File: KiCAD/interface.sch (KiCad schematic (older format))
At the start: 32 parts, among them P10 C3SB, P11 VSel_Vlv, P14 X_VALVE, P17 PUMP, P18 Pump_Cable, P34 VSel_Vlv2, P38 X_VALVE2, P7 GAGE_PR, P9 C3SB, Q1 BCP5416TA, Q2 BCP5416TA, Q3 BCP5416TA, Q4 BCP5416TA, U1 TXB0104D

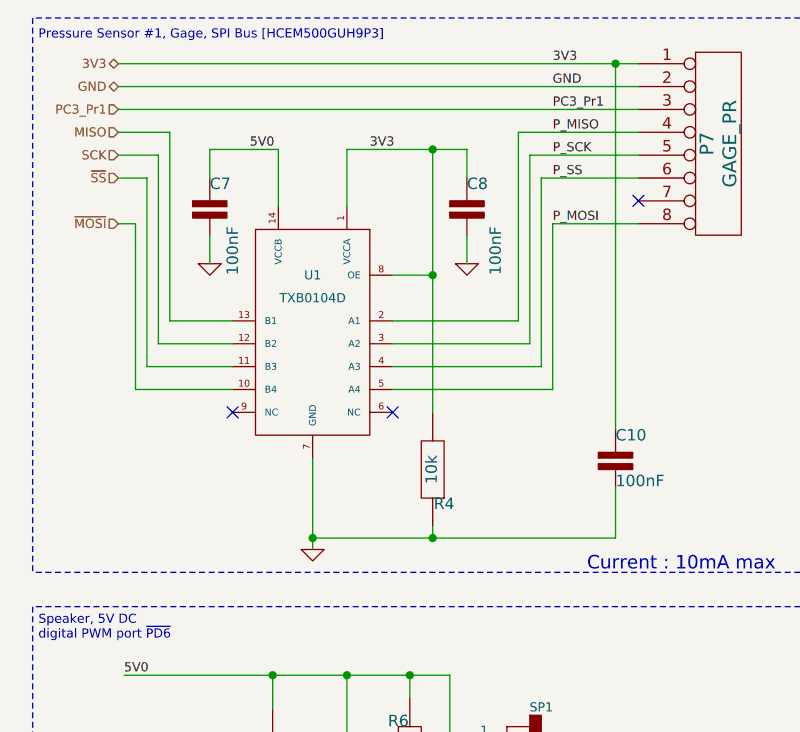
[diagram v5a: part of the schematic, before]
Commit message: layout finalized, needs a check for errors
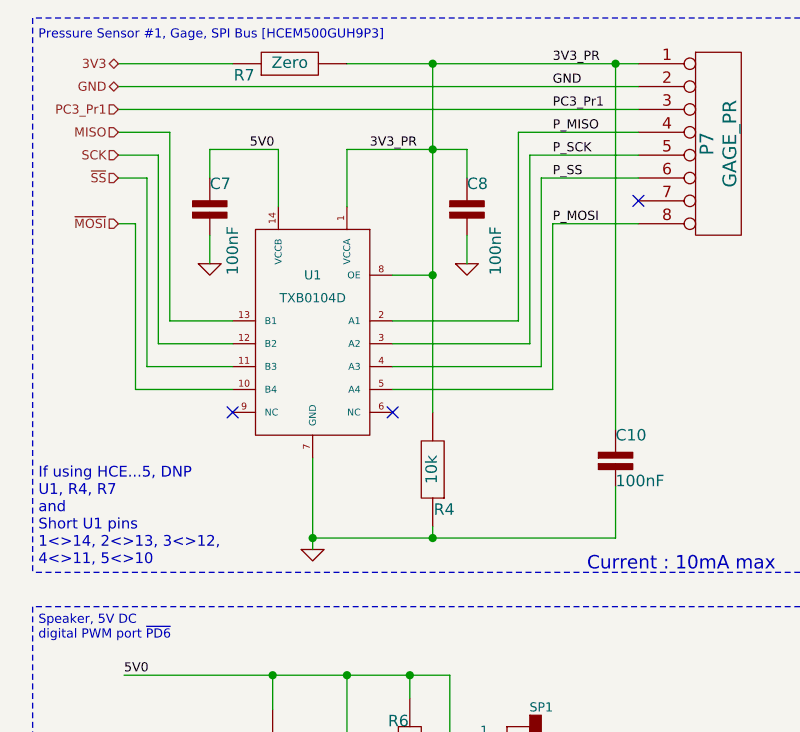
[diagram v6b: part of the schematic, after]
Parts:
- added R7: Zero, uCm:r_0805, symbol R
- U1: footprint uCm:TXB0104D -> uCm:TXB0104D_null
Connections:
- net 3V3: now also R7.1; no longer C10.1, C8.1, P7.1 (P1), R4.2, U1.1 (VCCA), U1.8 (OE)
- new net 3V3_PR: C10.1, C8.1, P7.1 (P1), R4.2, R7.2, U1.1 (VCCA), U1.8 (OE)
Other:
- note added: "If using HCE...5, DNP\nU1, R4, R7\nand\nShort U1 pins\n1<>14, 2<>13, 3<>12, \n4<>11, 5<>10"
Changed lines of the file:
@@
 	3325 875  1050 875
-Wire Wire Line
-	1050 775  3325 775
 Wire Wire Line
 	1050 975  3325 975
@@
 	1450 1525 1450 1650
 Wire Wire Line
-	2425 1150 2425 2300
+	2425 775  2425 2300
 Connection ~ 2425 1700
 Wire Notes Line
@@
 F 0 "U1" H 1900 2500 40  0000 C CNN
 F 1 "TXB0104D" H 1900 2400 40  0000 C CNN
-F 2 "uCm:TXB0104D" H 1900 2500 40  0001 C CNN
+F 2 "uCm:TXB0104D_null" H 1900 2500 40  0001 C CNN
 F 3 "" H 1900 2100 60  0001 C CNN
 F 4 "TXB0104DR" H 1900 2100 60  0001 C CNN "manf#"
@@
 U 1 1 50E2B821
 P 2425 2550
-F 0 "R4" H 2375 2700 50  0000 C CNN
+F 0 "R4" H 2375 2725 50  0000 C CNN
 F 1 "10k" V 2430 2550 50  0000 C CNN
 F 2 "uCm:r_0805" V 2530 2550 50  0001 C CNN
@@
 5V0
 Text Label 2150 1150 0    40   ~ 0
-3V3
+3V3_PR
 Text HLabel 4425 1300 0    40   BiDi ~ 0
 5V0
@@
 GND
 Text Label 2950 775  0    40   ~ 0
-3V3
+3V3_PR
 Text Notes 4500 6000 0    30   ~ 0
 Pump [P54E01R]\nFootprint
@@
 Text Notes 6200 4500 0    59   ~ 0
 Current : 200mA max
+Wire Wire Line
+	2050 775  3325 775
+$Comp
+L R R7
+U 1 1 5665D2FA
+P 1800 775
+F 0 "R7" V 1750 975 50  0000 C CNN
+F 1 "Zero" V 1805 775 50  0000 C CNN
+F 2 "uCm:r_0805" V 1905 775 50  0001 C CNN
+F 3 "" H 1800 775 60  0001 C CNN
+F 4 "RMCF0805ZT0R00" H 1800 775 60  0001 C CNN "manf#"
+	1    1800 775
+	0    -1   -1   0
+$EndComp
+Wire Wire Line
+	1550 775  1050 775
+Connection ~ 2425 775
+Text Notes 700  2975 0    47   ~ 0
+If using HCE...5, DNP\nU1, R4, R7\nand\nShort U1 pins\n1<>14, 2<>13, 3<>12, \n4<>11, 5<>10
 $EndSCHEMATC

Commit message: renamed uCm to mmM
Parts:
- C10, C11, C13, C14, C17, C29, C31, C7, C8, C9: footprint uCm:c_0805 -> mmM:c_0805
- C27: footprint uCm:C_ELCO_SMD_6x8 -> mmM:C_ELCO_SMD_6x8
- D1, D3, D9: footprint uCm:Diode-SMA -> mmM:Diode-SMA
- P10, P9: footprint uCm:pin_strip_4-90 -> mmM:pin_strip_4-90
- P11, P34: footprint uCm:Header_3 -> mmM:Header_3
- P14, P38: footprint uCm:X_Valve_2 -> mmM:X_Valve_2
- P17: footprint uCm:Pump_P54E01R_02 -> mmM:Pump_P54E01R_02
- P7: footprint uCm:HCEM500GUH9P3 -> mmM:HCEM500GUH9P3
- Q1, Q2, Q3, Q4: footprint uCm:SOT223 -> mmM:SOT223
- R4, R5, R6, R7: footprint uCm:r_0805 -> mmM:r_0805
- SP1: footprint uCm:Speaker -> mmM:Speaker
- U1: footprint uCm:TXB0104D_null -> mmM:TXB0104D_null
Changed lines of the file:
@@
 EESchema Schematic File Version 2
-LIBS:uCm
+LIBS:mmM
 LIBS:power
-LIBS:uCm-cache
+LIBS:mmM-cache
 EELAYER 25 0
 EELAYER END
@@
 F 0 "C27" V 3600 6350 50  0000 L CNN
 F 1 "100uF" V 3425 6350 50  0000 L CNN
-F 2 "uCm:C_ELCO_SMD_6x8" H 3150 6550 50  0001 C CNN
+F 2 "mmM:C_ELCO_SMD_6x8" H 3150 6550 50  0001 C CNN
 F 3 "" H 3550 6575 60  0001 C CNN
 F 4 "UWT1V101MCL1GS" V 3550 6575 60  0001 C CNN "manf#"
@@
 F 0 "P9" V 9525 1150 50  0000 C CNN
 F 1 "C3SB" V 9625 1150 50  0000 C CNN
-F 2 "uCm:pin_strip_4-90" H 9575 1150 60  0001 C CNN
+F 2 "mmM:pin_strip_4-90" H 9575 1150 60  0001 C CNN
 F 3 "" H 9575 1150 60  0001 C CNN
 F 4 "PREC004SAAN-RC" V 9575 1150 60  0001 C CNN "manf#"
@@
 F 0 "U1" H 1900 2500 40  0000 C CNN
 F 1 "TXB0104D" H 1900 2400 40  0000 C CNN
-F 2 "uCm:TXB0104D_null" H 1900 2500 40  0001 C CNN
+F 2 "mmM:TXB0104D_null" H 1900 2500 40  0001 C CNN
 F 3 "" H 1900 2100 60  0001 C CNN
 F 4 "TXB0104DR" H 1900 2100 60  0001 C CNN "manf#"
@@
 F 0 "R4" H 2375 2725 50  0000 C CNN
 F 1 "10k" V 2430 2550 50  0000 C CNN
-F 2 "uCm:r_0805" V 2530 2550 50  0001 C CNN
+F 2 "mmM:r_0805" V 2530 2550 50  0001 C CNN
 F 3 "" H 2425 2550 60  0001 C CNN
 F 4 "RMCF0805JT10K0" H 2425 2550 60  0001 C CNN "manf#"
@@
 F 0 "Q1" H 5125 1850 50  0000 C CNN
 F 1 "BCP5416TA" H 5025 1775 50  0000 C CNN
-F 2 "uCm:SOT223" H 5340 2025 30  0001 C CNN
+F 2 "mmM:SOT223" H 5340 2025 30  0001 C CNN
 F 3 "" H 5150 2025 60  0001 C CNN
 F 4 "BCP5416TA" H 5150 2025 60  0001 C CNN "manf#"
@@
 F 0 "P14" V 6900 1125 40  0000 C CNN
 F 1 "X_VALVE" V 7000 1125 40  0000 C CNN
-F 2 "uCm:X_Valve_2" H 6950 1125 60  0001 L CNN
+F 2 "mmM:X_Valve_2" H 6950 1125 60  0001 L CNN
 F 3 "" H 6950 1125 60  0001 C CNN
 F 4 "X-1-05-S-F" V 6950 1125 60  0001 C CNN "manf#"
@@
 F 0 "P7" V 3625 1125 60  0000 C CNN
 F 1 "GAGE_PR" V 3725 1125 60  0000 C CNN
-F 2 "uCm:HCEM500GUH9P3" V 3850 1125 60  0001 C CNN
+F 2 "mmM:HCEM500GUH9P3" V 3850 1125 60  0001 C CNN
 F 3 "" H 3675 1125 60  0001 C CNN
 F 4 "HCEM500GUH9P3" V 3675 1125 60  0001 C CNN "manf#"
@@
 F 0 "D1" V 4825 1450 40  0000 C CNN
 F 1 "ES1D-13-F" V 4725 1575 40  0000 C CNN
-F 2 "uCm:Diode-SMA" V 4850 1525 40  0001 C CNN
+F 2 "mmM:Diode-SMA" V 4850 1525 40  0001 C CNN
 F 3 "" H 4925 1375 60  0001 C CNN
 F 4 "ES1D-13-F" V 4925 1375 60  0001 C CNN "manf#"
@@
 F 0 "C17" H 3775 6700 50  0000 L CNN
 F 1 "100nF" H 3775 6500 50  0000 L CNN
-F 2 "uCm:c_0805" H 3775 6600 50  0001 C CNN
+F 2 "mmM:c_0805" H 3775 6600 50  0001 C CNN
 F 3 "" H 3775 6600 60  0001 C CNN
 F 4 "CL21B104KCC5PNC" H 3775 6600 60  0001 C CNN "manf#"
@@
 F 0 "C13" H 5500 2125 50  0000 L CNN
 F 1 "100nF" H 5500 1925 50  0000 L CNN
-F 2 "uCm:c_0805" H 5500 2025 50  0001 C CNN
+F 2 "mmM:c_0805" H 5500 2025 50  0001 C CNN
 F 3 "" H 5500 2025 60  0001 C CNN
 F 4 "CL21B104KCC5PNC" H 5500 2025 60  0001 C CNN "manf#"
@@
 F 0 "C11" H 10925 1225 50  0000 L CNN
 F 1 "100nF" H 10925 1025 50  0000 L CNN
-F 2 "uCm:c_0805" H 10925 1125 50  0001 C CNN
+F 2 "mmM:c_0805" H 10925 1125 50  0001 C CNN
 F 3 "" H 10925 1125 60  0001 C CNN
 F 4 "CL21B104KCC5PNC" H 10925 1125 60  0001 C CNN "manf#"
@@
 F 0 "C10" H 3225 2600 50  0000 L CNN
 F 1 "100nF" H 3225 2400 50  0000 L CNN
-F 2 "uCm:c_0805" H 3225 2500 50  0001 C CNN
+F 2 "mmM:c_0805" H 3225 2500 50  0001 C CNN
 F 3 "" H 3225 2500 60  0001 C CNN
 F 4 "CL21B104KCC5PNC" H 3225 2500 60  0001 C CNN "manf#"
@@
 F 0 "C9" H 9800 1225 50  0000 L CNN
 F 1 "100nF" H 9800 1025 50  0000 L CNN
-F 2 "uCm:c_0805" H 9800 1125 50  0001 C CNN
+F 2 "mmM:c_0805" H 9800 1125 50  0001 C CNN
 F 3 "" H 9800 1125 60  0001 C CNN
 F 4 "CL21B104KCC5PNC" H 9800 1125 60  0001 C CNN "manf#"
@@
 F 0 "C8" H 2575 1500 50  0000 L CNN
 F 1 "100nF" V 2700 1100 50  0000 L CNN
-F 2 "uCm:c_0805" H 2575 1400 50  0001 C CNN
+F 2 "mmM:c_0805" H 2575 1400 50  0001 C CNN
 F 3 "" H 2575 1400 60  0001 C CNN
 F 4 "CL21B104KCC5PNC" H 2575 1400 60  0001 C CNN "manf#"
@@
 F 0 "C7" H 1450 1500 50  0000 L CNN
 F 1 "100nF" V 1550 1100 50  0000 L CNN
-F 2 "uCm:c_0805" H 1450 1400 50  0001 C CNN
+F 2 "mmM:c_0805" H 1450 1400 50  0001 C CNN
 F 3 "" H 1450 1400 60  0001 C CNN
 F 4 "CL21B104KCC5PNC" H 1450 1400 60  0001 C CNN "manf#"
@@
 F 0 "P10" V 10650 1150 50  0000 C CNN
 F 1 "C3SB" V 10750 1150 50  0000 C CNN
-F 2 "uCm:pin_strip_4-90" V 10850 1150 50  0001 C CNN
+F 2 "mmM:pin_strip_4-90" V 10850 1150 50  0001 C CNN
 F 3 "" H 10700 1150 60  0001 C CNN
 F 4 "PREC004SAAN-RC" V 10700 1150 60  0001 C CNN "manf#"
@@
 F 0 "P11" V 4325 1025 50  0000 C CNN
 F 1 "VSel_Vlv" V 4425 1025 40  0000 C CNN
-F 2 "uCm:Header_3" V 4525 1025 40  0001 C CNN
+F 2 "mmM:Header_3" V 4525 1025 40  0001 C CNN
 F 3 "" H 4375 1025 60  0001 C CNN
 F 4 "PREC003SAAN-RC" V 4375 1025 60  0001 C CNN "manf#"
@@
 F 0 "Q2" V 2375 6925 50  0000 C CNN
 F 1 "BCP5416TA" V 2375 6500 50  0000 C CNN
-F 2 "uCm:SOT223" H 2665 6825 30  0001 C CNN
+F 2 "mmM:SOT223" H 2665 6825 30  0001 C CNN
 F 3 "" H 2475 6825 60  0001 C CNN
 F 4 "BCP5416TA" V 2475 6825 60  0001 C CNN "manf#"
@@
 F 0 "R5" H 3100 6150 50  0000 C CNN
 F 1 "4k7" V 3055 5975 50  0000 C CNN
-F 2 "uCm:r_0805" V 3155 5975 50  0001 C CNN
+F 2 "mmM:r_0805" V 3155 5975 50  0001 C CNN
 F 3 "" H 3050 5975 60  0001 C CNN
 F 4 "RMCF0805JT4K70" H 3050 5975 60  0001 C CNN "manf#"
@@
 F 0 "C29" H 3075 6675 50  0000 L CNN
 F 1 "100nF" H 3050 6500 50  0000 L CNN
-F 2 "uCm:c_0805" H 3050 6600 50  0001 C CNN
+F 2 "mmM:c_0805" H 3050 6600 50  0001 C CNN
 F 3 "" H 3050 6600 60  0001 C CNN
 F 4 "CL21B104KCC5PNC" H 3050 6600 60  0001 C CNN "manf#"
@@
 F 0 "Q3" H 5125 3900 50  0000 C CNN
 F 1 "BCP5416TA" H 5025 3825 50  0000 C CNN
-F 2 "uCm:SOT223" H 5340 4075 30  0001 C CNN
+F 2 "mmM:SOT223" H 5340 4075 30  0001 C CNN
 F 3 "" H 5150 4075 60  0001 C CNN
 F 4 "BCP5416TA" H 5150 4075 60  0001 C CNN "manf#"
@@
 F 0 "P38" V 6925 3175 40  0000 C CNN
 F 1 "X_VALVE2" V 7025 3175 40  0000 C CNN
-F 2 "uCm:X_Valve_2" H 6975 3175 60  0001 L CNN
+F 2 "mmM:X_Valve_2" H 6975 3175 60  0001 L CNN
 F 3 "" H 6975 3175 60  0001 C CNN
 F 4 "X-1-05-S-F" V 6975 3175 60  0001 C CNN "manf#"
@@
 F 0 "D9" V 4825 3500 40  0000 C CNN
 F 1 "ES1D-13-F" V 4750 3625 40  0000 C CNN
-F 2 "uCm:Diode-SMA" V 4850 3575 40  0001 C CNN
+F 2 "mmM:Diode-SMA" V 4850 3575 40  0001 C CNN
 F 3 "" H 4925 3425 60  0001 C CNN
 F 4 "ES1D-13-F" V 4925 3425 60  0001 C CNN "manf#"
@@
 F 0 "C31" H 5500 4175 50  0000 L CNN
 F 1 "100nF" H 5500 3975 50  0000 L CNN
-F 2 "uCm:c_0805" H 5500 4075 50  0001 C CNN
+F 2 "mmM:c_0805" H 5500 4075 50  0001 C CNN
 F 3 "" H 5500 4075 60  0001 C CNN
 F 4 "CL21B104KCC5PNC" H 5500 4075 60  0001 C CNN "manf#"
@@
 F 0 "P34" V 4325 3075 50  0000 C CNN
 F 1 "VSel_Vlv2" V 4425 3075 40  0000 C CNN
-F 2 "uCm:Header_3" V 4525 3075 40  0001 C CNN
+F 2 "mmM:Header_3" V 4525 3075 40  0001 C CNN
 F 3 "" H 4375 3075 60  0001 C CNN
 F 4 "PREC003SAAN-RC" V 4375 3075 60  0001 C CNN "manf#"
@@
 F 0 "C14" H 2050 4700 50  0000 L CNN
 F 1 "100nF" H 2050 4500 50  0000 L CNN
-F 2 "uCm:c_0805" H 2050 4600 50  0001 C CNN
+F 2 "mmM:c_0805" H 2050 4600 50  0001 C CNN
 F 3 "" H 2050 4600 60  0001 C CNN
 F 4 "CL21B104KCC5PNC" H 2050 4600 60  0001 C CNN "manf#"
@@
 F 0 "Q4" H 1600 4350 50  0000 C CNN
 F 1 "BCP5416TA" H 1500 4275 50  0000 C CNN
-F 2 "uCm:SOT223" H 1815 4525 30  0001 C CNN
+F 2 "mmM:SOT223" H 1815 4525 30  0001 C CNN
 F 3 "" H 1625 4525 60  0001 C CNN
 F 4 "BCP5416TA" H 1625 4525 60  0001 C CNN "manf#"
@@
 F 0 "D3" V 1625 3875 40  0000 C CNN
 F 1 "ES1D-13-F" V 1550 4000 40  0000 C CNN
-F 2 "uCm:Diode-SMA" V 1650 3950 40  0001 C CNN
+F 2 "mmM:Diode-SMA" V 1650 3950 40  0001 C CNN
 F 3 "" H 1725 3800 60  0001 C CNN
 F 4 "ES1D-13-F" V 1725 3800 60  0001 C CNN "manf#"
@@
 F 0 "R6" H 2275 3950 50  0000 C CNN
 F 1 "1k" V 2330 3800 50  0000 C CNN
-F 2 "uCm:r_0805" V 2430 3800 50  0001 C CNN
+F 2 "mmM:r_0805" V 2430 3800 50  0001 C CNN
 F 3 "" H 2325 3800 60  0001 C CNN
 F 4 "RMCF0805JT1K00" H 2325 3800 60  0001 C CNN "manf#"
@@
 F 0 "SP1" H 2900 3960 40  0000 C CNN
 F 1 "BUZZER" H 2960 3580 40  0000 C CNN
-F 2 "uCm:Speaker" H 2850 3775 60  0001 C CNN
+F 2 "mmM:Speaker" H 2850 3775 60  0001 C CNN
 F 3 "" H 2850 3775 60  0000 C CNN
 F 4 "PS1240P02BT" H 2850 3775 60  0001 C CNN "manf#"
@@
 F 0 "P17" V 4550 5550 40  0000 C CNN
 F 1 "PUMP" V 4650 5550 40  0000 C CNN
-F 2 "uCm:Pump_P54E01R_02" H 4600 5500 60  0001 C CNN
+F 2 "mmM:Pump_P54E01R_02" H 4600 5500 60  0001 C CNN
 F 3 "http://www.xavitech.com/products" H 4600 5500 60  0001 C CNN
 F 4 "P54E01R" V 4600 5550 60  0001 C CNN "manf#"
@@
 F 0 "R7" V 1750 975 50  0000 C CNN
 F 1 "Zero" V 1805 775 50  0000 C CNN
-F 2 "uCm:r_0805" V 1905 775 50  0001 C CNN
+F 2 "mmM:r_0805" V 1905 775 50  0001 C CNN
 F 3 "" H 1800 775 60  0001 C CNN
 F 4 "RMCF0805ZT0R00" H 1800 775 60  0001 C CNN "manf#"
